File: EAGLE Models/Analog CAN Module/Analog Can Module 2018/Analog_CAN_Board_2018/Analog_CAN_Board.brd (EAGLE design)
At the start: 90 x 38 mm, 121 parts, among them IC1 AT90CAN128, IC10 OPA725DBV, IC11 OPA725DBV, IC12 OPA725DBV, IC13 OPA725DBV, IC2 MCP2551SO8, IC3 NUP2105L, IC4 OPA725DBV, IC5 FT232RL, IC6 MAX680CSA, IC7 OPA725DBV, IC8 OPA725DBV, IC9 OPA725DBV, Q1 56P2859, U11 LTC2053

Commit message: CAN Boards Finished
Passes DFM!
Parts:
- removed D1: 1N5819, diode:DO41-7.6
- added U$4: 1N5819, diode:1N5819SM
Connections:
- net 12V: now also U$4.P$1; no longer D1.A
- net 5V_REG_IN: now also U$4.P$2; no longer D1.C
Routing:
- net VCC: track 230.6 -> 199.4 mm, vias 10 -> 8
- net 12V: track 65.0 -> 67.8 mm
- net 5V_REG_IN: track 9.83 -> 7.17 mm
- net N$28: track 6.51 -> 8.70 mm
- net A8O: track 28.3 -> 30.0 mm

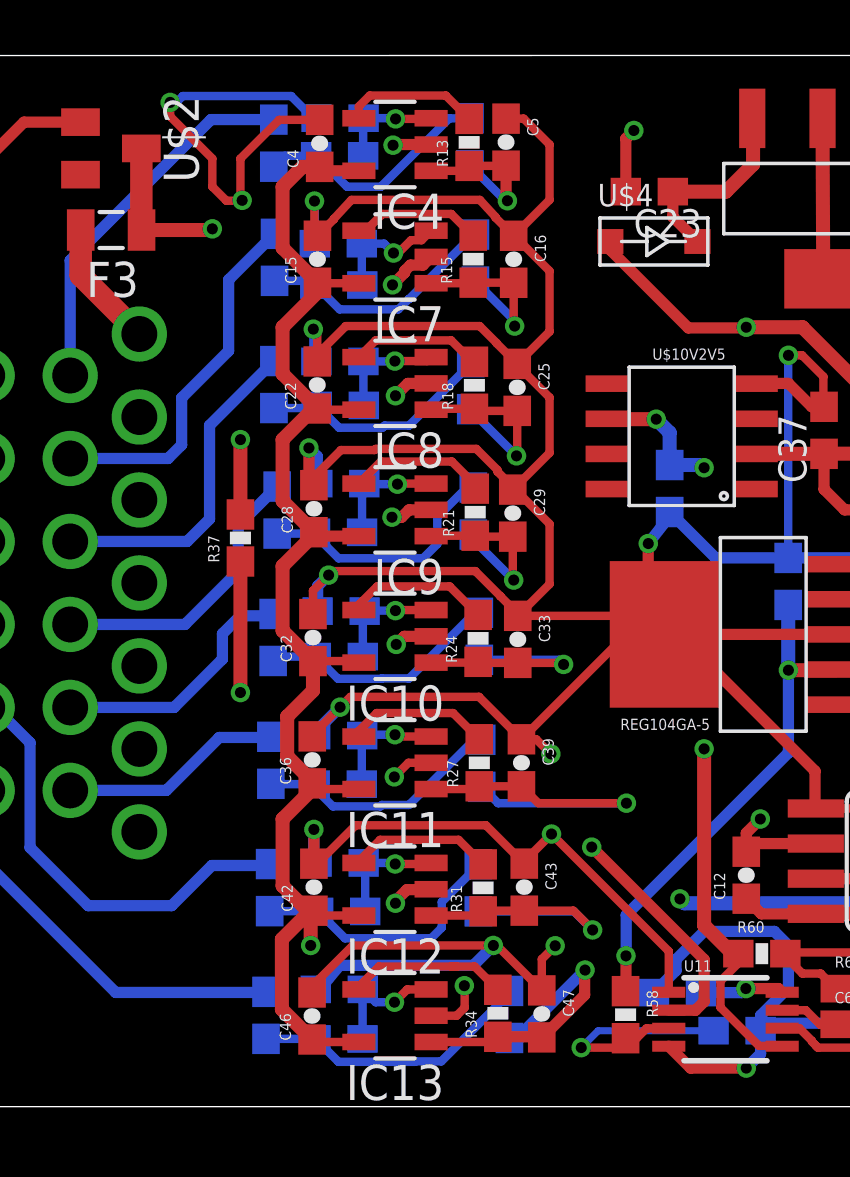
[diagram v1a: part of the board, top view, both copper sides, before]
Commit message: Last minute CAN Board revision
- added 0 ohm resistors for filters and adjusted q to 2
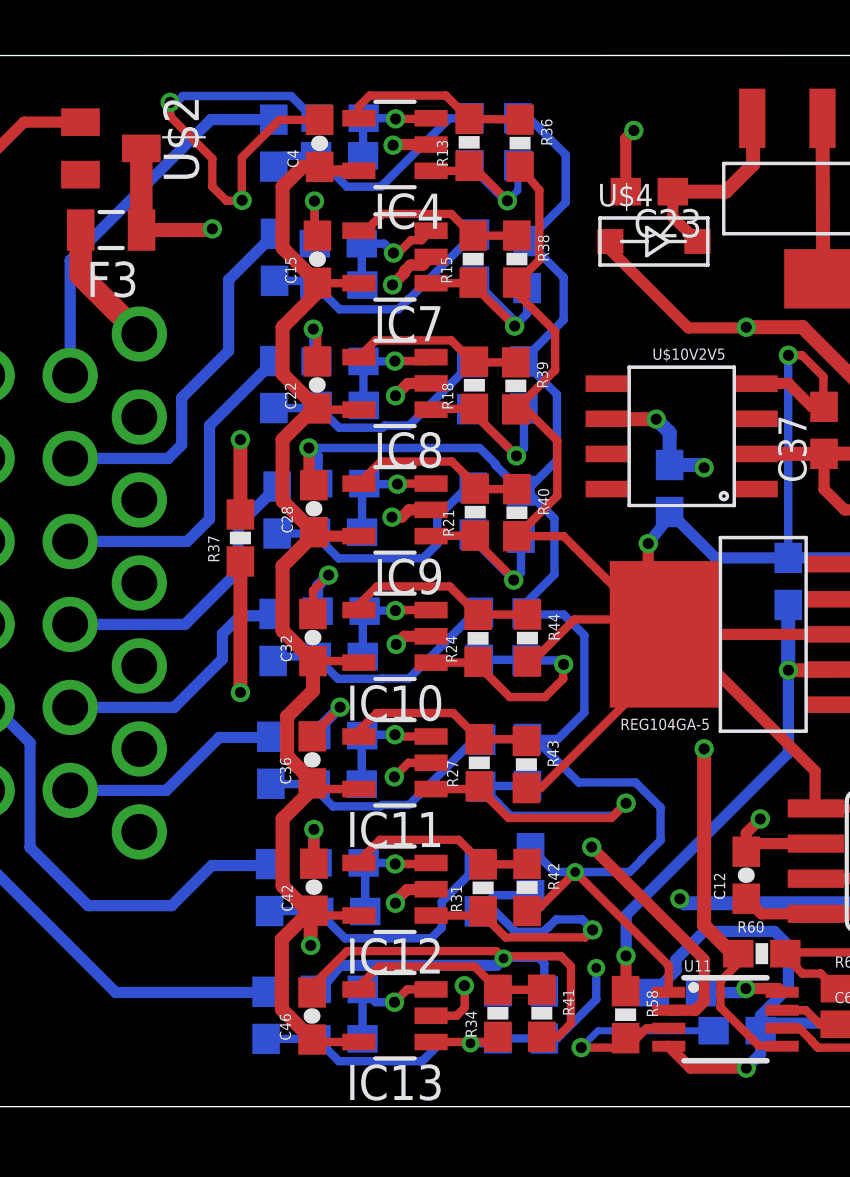
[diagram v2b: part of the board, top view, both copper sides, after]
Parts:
- added R36, R38, R39, R40, R41, R42, R43, R44: 0, SparkFun-Resistors:0603-RES
- C14, C21, C27, C3, C35, C41, C45: value .1uF -> .0047uF
- C17, C26, C30, C44, C48, C6: value .33uF -> .1uF
- R1, R14, R17, R20, R26, R30, R33: value 3.9k -> 22k
- R16, R19, R22, R28, R29, R32, R35: value 5.1k -> 62k
- moved C43 0.60 mm to (31.3, 23.5), flipped to the bottom
- moved C16 0.52 mm to (31.2, 45.4), flipped to the bottom
- moved C5 0.43 mm to (30.9, 49.9), flipped to the bottom
- moved C48 0.42 mm to (30.1, 18.3)
- moved C33 0.32 mm to (31.2, 32.0), flipped to the bottom
- moved C29 0.30 mm to (31.0, 36.4), flipped to the bottom
- moved C25 0.26 mm to (31.1, 41.1), flipped to the bottom
- moved C39 0.22 mm to (31.2, 27.4), flipped to the bottom
- moved C47 0.10 mm to (31.8, 18.3), flipped to the bottom
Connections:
- net AGND: now also R36.2, R38.2, R39.2, R40.2, R41.2, R42.2, R43.2, R44.2
- net N$19: now also R36.1
- net N$26: now also R38.1
- net N$31: now also R39.1
- net N$38: now also R40.1
- net N$41: now also R44.1
- net N$44: now also R43.1
- net N$47: now also R42.1
- net N$50: now also R41.1
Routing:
- net AGND: track 299.8 -> 313.1 mm, vias 19 -> 17
- net N$51: track 10.3 -> 7.12 mm
- net A7O: track 34.7 -> 37.5 mm
- net A6O: track 36.7 -> 39.1 mm
- net A8O: track 30.0 -> 27.8 mm, vias 2 -> 3
- net N$41: track 5.20 -> 7.23 mm
- net N$19: track 4.93 -> 6.77 mm
- net N$44: track 5.22 -> 6.95 mm
- net A5O: track 29.8 -> 31.4 mm
- net N$47: track 5.25 -> 6.84 mm
- net N$26: track 4.71 -> 6.29 mm
- net N$31: track 4.75 -> 6.32 mm
- net N$38: track 5.02 -> 6.54 mm
- net N$50: track 5.97 -> 7.37 mm
- net A3O: track 32.1 -> 33.2 mm
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
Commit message: Analog CAN Board Update
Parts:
- moved R37 15.5 mm to (5.52, 38.0)
- moved R43 1.17 mm to (31.5, 28.5)
- moved C39 1.15 mm to (31.7, 28.5)
- moved R28 0.89 mm to (21.2, 49.5), turned to 0 degrees
- moved R42 0.87 mm to (31.5, 23.7)
- moved C44 0.58 mm to (29.8, 23.3)
- moved R36 0.51 mm to (30.8, 50.3)
- moved C40 0.46 mm to (29.8, 27.8)
- moved R13 0.44 mm to (29.2, 50.3)
- moved C5 0.42 mm to (30.9, 50.3)
- moved C43 0.41 mm to (31.6, 23.7)
- moved R27 0.40 mm to (29.6, 27.8)
- moved R31 0.40 mm to (29.6, 23.3)
- moved C15 0.38 mm to (23.6, 45.3)
- moved C6 0.37 mm to (29.1, 50.3)
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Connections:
- net AGND: now also U$3.B22, U$3.B23, U$3.B24; no longer U$3.B14, U$3.B15
- net DGND: now also U$3.B14, U$3.B15; no longer U$3.B22, U$3.B23, U$3.B24
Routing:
- net DGND: track 261.5 -> 41.1 mm, vias 12 -> 21
- net AGND: track 313.1 -> 93.2 mm, vias 17 -> 29
- net VCC: track 199.4 -> 51.2 mm, vias 8 -> 11
- net 12V: track 67.8 -> 57.7 mm
- net A6O: track 39.1 -> 33.0 mm, vias 2 -> 1
- net TX: track 24.4 -> 18.5 mm
- net +10V: track 79.3 -> 73.8 mm, vias 3 -> 2
- net SG: track 32.1 -> 37.2 mm, vias 1 -> 4
- net RX: track 28.1 -> 24.2 mm, vias 2 -> 1
- net A7O: track 37.5 -> 34.0 mm, vias 2 -> 1
- net N$51: track 7.12 -> 9.97 mm
- net 2V5REF: track 28.2 -> 30.4 mm
- net A1: track 13.6 -> 11.9 mm
- net A5O: track 31.4 -> 29.9 mm, vias 2 -> 1
- net A2O: track 34.0 -> 32.5 mm, vias 2 -> 1
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
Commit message: Analog CAN Update
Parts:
- R11, R12: value .01 Ohm -> 0; device Vishay_By_element14_Batch_1:RESC1608X60N -> SparkFun-Resistors:0603-RES
- moved R1 1.78 mm to (24.4, 51.2)
- moved C24 1.32 mm to (47.2, 42.8), turned to 0 degrees
- moved C3 1.02 mm to (24.4, 49.7)
- moved C4 0.94 mm to (23.0, 50.5), turned to 270 degrees
- moved R12 0.35 mm to (49.3, 28.8)
- moved C46 0.25 mm to (23.4, 18.5)
- moved C47 0.25 mm to (31.8, 18.6)
- moved C48 0.25 mm to (30.1, 18.6)
- moved IC13 0.25 mm to (26.4, 18.5)
- moved R33 0.25 mm to (24.4, 17.7)
- moved R35 0.25 mm to (21.8, 18.6)
- moved R41 0.25 mm to (31.7, 18.6)
- moved C45 0.25 mm to (24.4, 19.5)
- moved R34 0.25 mm to (30.1, 18.6)
- moved R11 0.22 mm to (51.7, 28.0)
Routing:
- net AGND: track 93.2 -> 87.7 mm, vias 29 -> 28
- net +10V: track 73.8 -> 78.4 mm
- net VCC: track 51.2 -> 55.6 mm, vias 11 -> 14
- net CAN_H: track 59.4 -> 61.6 mm
- net CAN_L: track 54.2 -> 56.3 mm
- net N$5: track 8.60 -> 9.71 mm
- net -10V: track 87.2 -> 88.3 mm

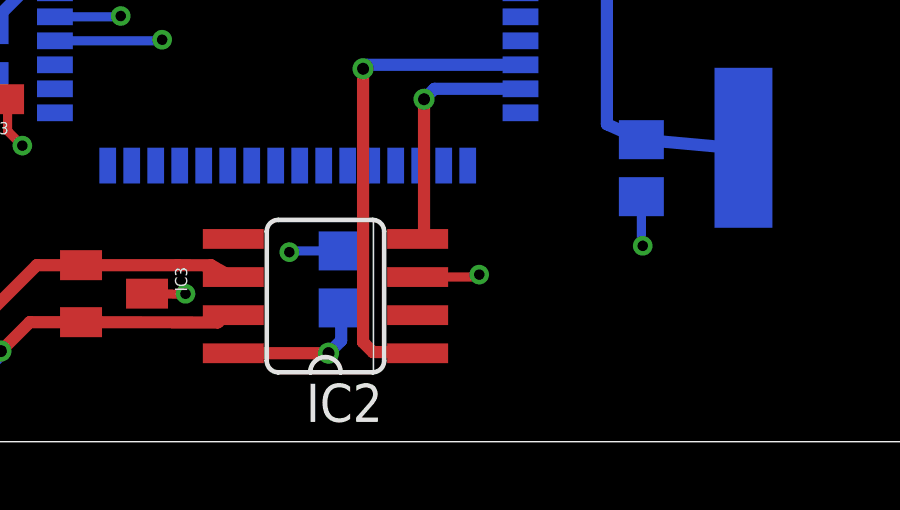
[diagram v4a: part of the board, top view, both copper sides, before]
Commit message: Fixed ground issue on the can transceiver
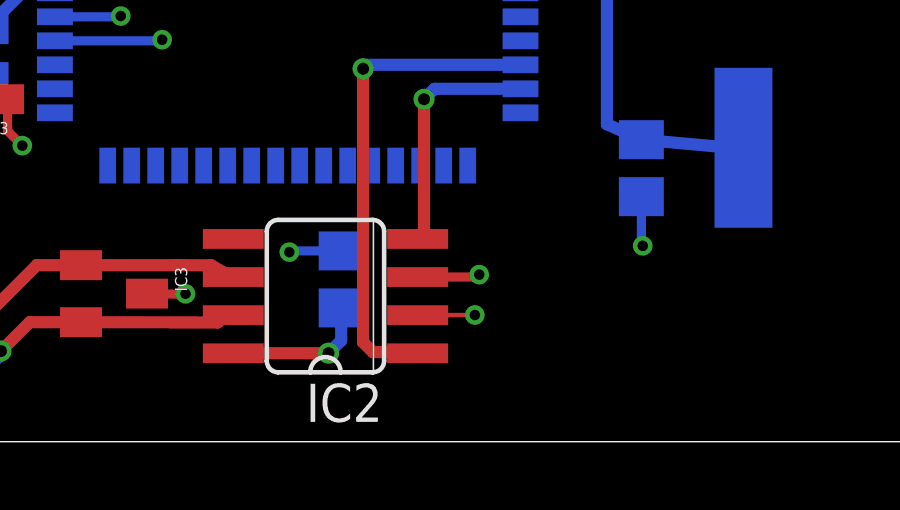
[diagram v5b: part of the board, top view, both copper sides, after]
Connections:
- net AGND: no longer IC2.2
- net DGND: now also IC2.2
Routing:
- net DGND: track 40.8 -> 42.8 mm, vias 21 -> 22
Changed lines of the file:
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@@
 <?xml version="1.0" encoding="utf-8"?>
 <!DOCTYPE eagle SYSTEM "eagle.dtd">
-<eagle version="8.3.2">
+<eagle version="8.4.3">
 <drawing>
 <settings>
@@
 <param name="dpMaxLengthDifference" value="10mm"/>
 <param name="dpGapFactor" value="2.5"/>
-<param name="checkGrid" value="0"/>
 <param name="checkAngle" value="0"/>
 <param name="checkFont" value="1"/>
 <param name="checkRestrict" value="1"/>
+<param name="checkStop" value="0"/>
 <param name="useDiameter" value="13"/>
 <param name="maxErrors" value="50"/>
@@
 <contactref element="C47" pad="1"/>
 <contactref element="R37" pad="1"/>
-<contactref element="IC2" pad="2"/>
 <contactref element="R36" pad="2"/>
 <contactref element="R44" pad="2"/>
@@
 <wire x1="23.85821875" y1="48.643" x2="23.85821875" y2="49.4445375" width="0.4064" layer="16"/>
 <wire x1="23.85821875" y1="49.4445375" x2="23.5809875" y2="49.72176875" width="0.4064" layer="16"/>
-<wire x1="52.65" y1="24.87" x2="65.8274" y2="19.219" width="0" layer="19" extent="1-1"/>
 </signal>
 <signal name="N$18">
@@
 <contactref element="U$3" pad="B14"/>
 <contactref element="U$3" pad="B15"/>
+<contactref element="IC2" pad="2"/>
+<wire x1="65.8274" y1="19.219" x2="67.72791875" y2="19.219" width="0.1524" layer="1"/>
+<wire x1="67.72791875" y1="19.219" x2="67.732909375" y2="19.223990625" width="0.1524" layer="1"/>
+<via x="67.732909375" y="19.223990625" extent="1-16" drill="0.35"/>
+<wire x1="68.499990625" y1="19.223990625" x2="68.58" y2="19.304" width="0.1524" layer="6"/>
 </signal>
 <signal name="A1O">

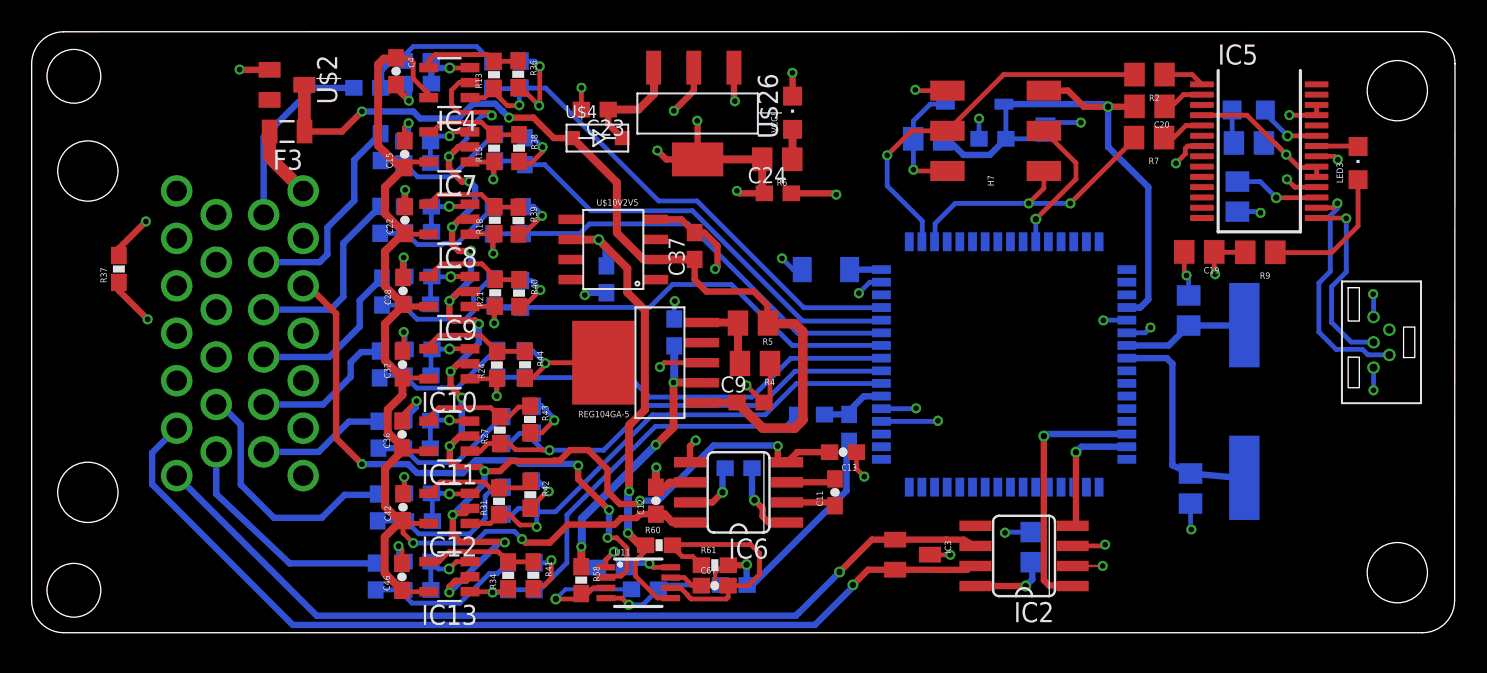
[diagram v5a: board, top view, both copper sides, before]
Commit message: Analog CAN Board Updates/Reference designators
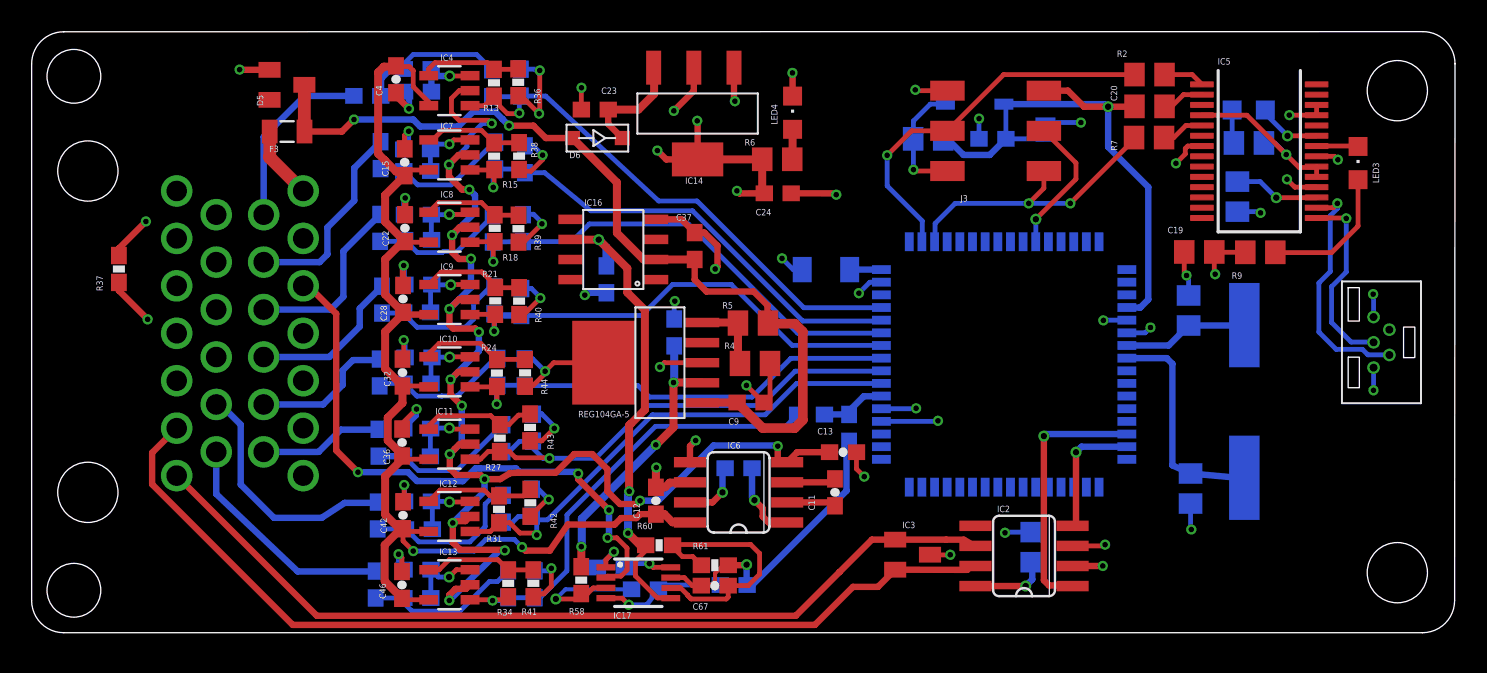
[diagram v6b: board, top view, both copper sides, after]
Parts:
- IC15: value REG-104GA-5 -> IC15
- moved C14 0.51 mm to (24.4, 45.6)
- moved C16 0.51 mm to (31.2, 44.9)
- moved C21 0.51 mm to (24.4, 41.4)
- moved C28 0.51 mm to (23.5, 36.1)
- moved C3 0.51 mm to (24.4, 49.2)
- moved C30 0.51 mm to (29.2, 36.0)
- moved C4 0.51 mm to (23.0, 50.0)
- moved C42 0.51 mm to (23.5, 22.4)
- moved C46 0.51 mm to (23.4, 18.0)
- moved C47 0.51 mm to (31.8, 18.1)
- moved C48 0.51 mm to (30.1, 18.1)
- moved IC13 0.51 mm to (26.4, 18.0)
- moved IC8 0.51 mm to (26.4, 40.6)
- moved IC9 0.51 mm to (26.4, 36.1)
- moved R13 0.51 mm to (29.2, 49.8)
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- renumbered H7 to J3, U$1 to J1, U$10V2V5 to IC16, U$2 to D5, U$26 to IC14, U$3 to J2, U$4 to D6, U$5 to IC15, U11 to IC17, VCC! to LED4
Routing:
- net AGND: track 87.7 -> 88.4 mm
- net A3: track 12.1 -> 11.5 mm
- net A4: track 10.5 -> 10.0 mm
- net A2: track 13.3 -> 12.7 mm
- net A8O: track 28.5 -> 29.0 mm
- net CAN_H: track 61.6 -> 61.5 mm, vias 1 -> 0
- net CAN_L: vias 1 -> 0
